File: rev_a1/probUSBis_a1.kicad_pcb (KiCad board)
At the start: 2 copper layers, 44.5 x 22.9 mm, 25 parts, among them CON1 USB-MINI-B, IC1 ATTINY85-P, P1 USB_A_MALE, P2 CONN_8, P3 CONN_4, U1 LM78L05ACZ

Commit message: added oshw logo to board
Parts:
- added G***: LOGO, LOGO, B.Cu at (118.1, 97.8)
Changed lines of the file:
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@@
     (tracks 183)
     (zones 0)
-    (modules 25)
+    (modules 26)
     (nets 21)
   )
@@
       (xy 2.71018 0) (xy 2.71018 1.016) (xy 2.71018 2.032) (xy 2.71018 2.032)) (layer B.SilkS) (width 0.00254))
   )
+  (module LOGO (layer B.Cu)
+    (at 118.11 97.79)
+    (fp_text reference G*** (at 0 -5.334) (layer B.SilkS) hide
+      (effects (font (thickness 0.3048)) (justify mirror))
+    )
+    (fp_text value LOGO (at 0 5.334) (layer B.SilkS) hide
+      (effects (font (thickness 0.3048)) (justify mirror))
+    )
+    (fp_poly (pts (xy 5.461 -4.53136) (xy 0.0635 -4.51104) (xy -5.334 -4.48818) (xy -5.35686 0.10414)
+      (xy -5.37718 4.699) (xy -5.3975 0.0635) (xy -5.41782 -4.572) (xy 0.02032 -4.55168)
+      (xy 5.461 -4.53136) (xy 5.461 -4.53136)) (layer B.SilkS) (width 0.00254))
+    (fp_poly (pts (xy 4.572 1.0922) (xy 4.2545 1.14808) (xy 3.86588 1.21666) (xy 3.60934 1.27254)
+      (xy 3.44678 1.34112) (xy 3.34264 1.44272) (xy 3.26136 1.59766) (xy 3.175 1.80848)
+      (xy 2.9718 2.30632) (xy 3.32486 2.80416) (xy 3.67538 3.302) (xy 3.25882 3.72364)
+      (xy 3.04292 3.93446) (xy 2.8702 4.08686) (xy 2.77622 4.14782) (xy 2.77368 4.14782)
+      (xy 2.67462 4.10464) (xy 2.4765 3.99034) (xy 2.24282 3.84048) (xy 1.98628 3.67538)
+      (xy 1.8161 3.59664) (xy 1.68148 3.58902) (xy 1.53416 3.63474) (xy 1.52146 3.63982)
+      (xy 1.34112 3.70332) (xy 1.2446 3.71602) (xy 1.23952 3.71348) (xy 1.20142 3.62712)
+      (xy 1.10998 3.4163) (xy 0.98298 3.10896) (xy 0.83058 2.74066) (xy 0.81788 2.70764)
+      (xy 0.41656 1.73482) (xy 0.63754 1.55702) (xy 0.96012 1.2065) (xy 1.14554 0.80772)
+      (xy 1.19634 0.38862) (xy 1.11252 -0.01778) (xy 0.89916 -0.381) (xy 0.55626 -0.66548)
+      (xy 0.508 -0.69088) (xy 0.08636 -0.83058) (xy -0.3302 -0.82042) (xy -0.7112 -0.67818)
+      (xy -1.0287 -0.42418) (xy -1.25222 -0.07366) (xy -1.35128 0.3556) (xy -1.35382 0.43942)
+      (xy -1.32588 0.82296) (xy -1.21412 1.11252) (xy -0.9906 1.38176) (xy -0.88138 1.48082)
+      (xy -0.59182 1.73482) (xy -0.98044 2.667) (xy -1.13792 3.0353) (xy -1.27762 3.34772)
+      (xy -1.38176 3.5687) (xy -1.4351 3.66522) (xy -1.5494 3.683) (xy -1.72212 3.62966)
+      (xy -1.85674 3.58394) (xy -1.99136 3.59664) (xy -2.16916 3.683) (xy -2.41046 3.83794)
+      (xy -2.65938 3.99542) (xy -2.85242 4.10718) (xy -2.94386 4.14782) (xy -3.03276 4.09194)
+      (xy -3.20294 3.94462) (xy -3.41884 3.73634) (xy -3.429 3.72618) (xy -3.84302 3.302)
+      (xy -3.49504 2.79654) (xy -3.14452 2.28854) (xy -3.36042 1.78562) (xy -3.48488 1.51384)
+      (xy -3.58648 1.3589) (xy -3.71094 1.28016) (xy -3.8989 1.23952) (xy -3.97002 1.22936)
+      (xy -4.3307 1.17602) (xy -4.55676 1.12268) (xy -4.68122 1.03886) (xy -4.73202 0.89154)
+      (xy -4.74218 0.65024) (xy -4.74218 0.45974) (xy -4.74218 -0.16256) (xy -4.42468 -0.25146)
+      (xy -4.15544 -0.30988) (xy -3.91668 -0.34036) (xy -3.89382 -0.34036) (xy -3.70078 -0.36068)
+      (xy -3.56108 -0.4445) (xy -3.43916 -0.61976) (xy -3.30454 -0.90678) (xy -3.11658 -1.3462)
+      (xy -3.47726 -1.86182) (xy -3.84048 -2.37998) (xy -3.3909 -2.83464) (xy -2.93878 -3.29184)
+      (xy -2.39268 -2.92354) (xy -1.84658 -2.55778) (xy -1.4097 -2.75844) (xy -0.97282 -2.9591)
+      (xy -0.85344 -3.59918) (xy -0.73152 -4.2418) (xy -0.09652 -4.2164) (xy 0.54102 -4.191)
+      (xy 0.6731 -3.56616) (xy 0.80518 -2.94132) (xy 1.2446 -2.74828) (xy 1.68402 -2.55524)
+      (xy 2.21742 -2.92862) (xy 2.75082 -3.29946) (xy 3.20548 -2.84734) (xy 3.66014 -2.39268)
+      (xy 3.30454 -1.86944) (xy 2.95148 -1.3462) (xy 3.14198 -0.88646) (xy 3.25628 -0.62738)
+      (xy 3.37058 -0.47244) (xy 3.53314 -0.38354) (xy 3.79222 -0.32512) (xy 3.937 -0.29972)
+      (xy 4.2545 -0.24638) (xy 4.44246 -0.18542) (xy 4.53644 -0.07366) (xy 4.56946 0.127)
+      (xy 4.572 0.45466) (xy 4.572 0.46736) (xy 4.572 1.0922) (xy 4.572 1.0922)) (layer B.SilkS) (width 0.00254))
+  )
   (gr_text SCK (at 143.51 99.06 270) (layer B.SilkS)
     (effects (font (size 0.4 0.4) (thickness 0.1)) (justify mirror))
@@
     (effects (font (size 0.8 0.8) (thickness 0.16)) (justify mirror))
   )
-  (gr_text github.com/emdarcher/probUSBis_hardware (at 113.03 102.87 90) (layer B.SilkS)
+  (gr_text github.com/emdarcher/probUSBis_hardware (at 111.76 102.87 90) (layer B.SilkS)
     (effects (font (size 0.6 0.6) (thickness 0.12)) (justify mirror))
   )

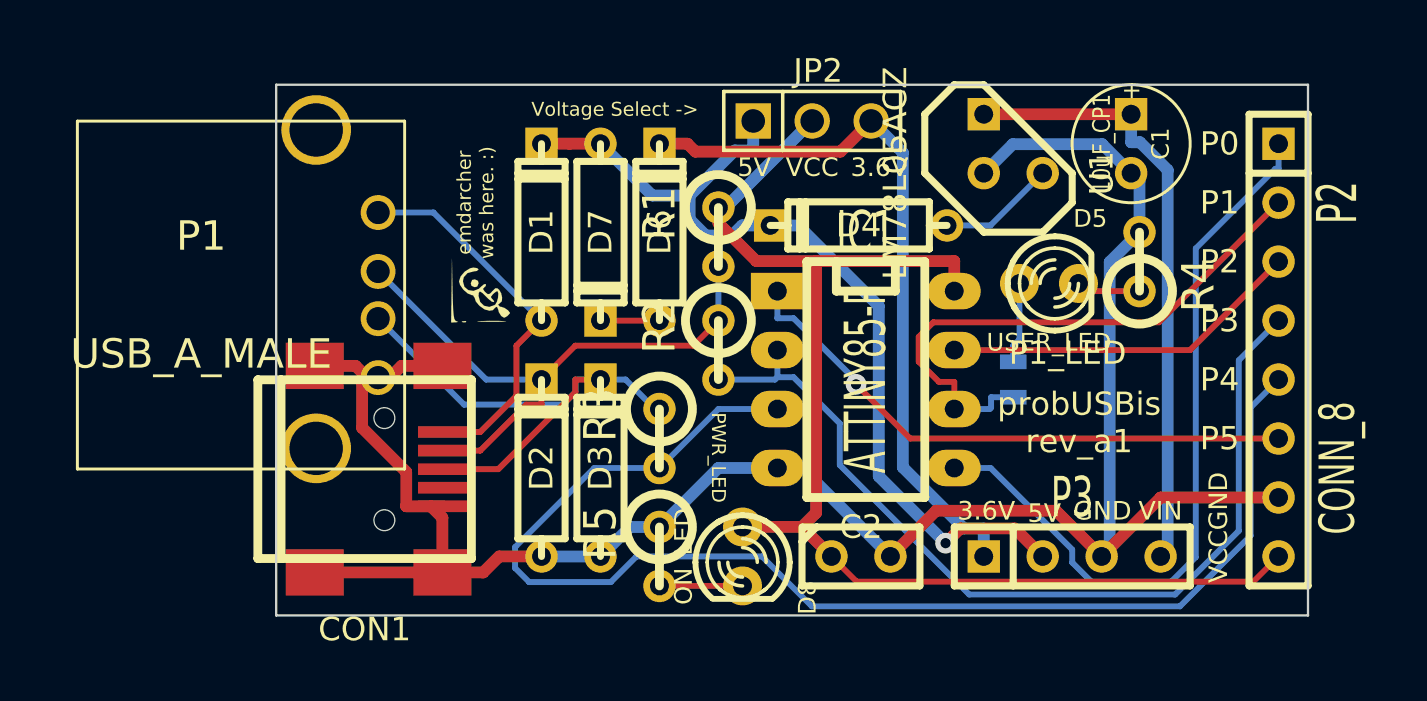
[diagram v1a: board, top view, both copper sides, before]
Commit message: added a ground fill
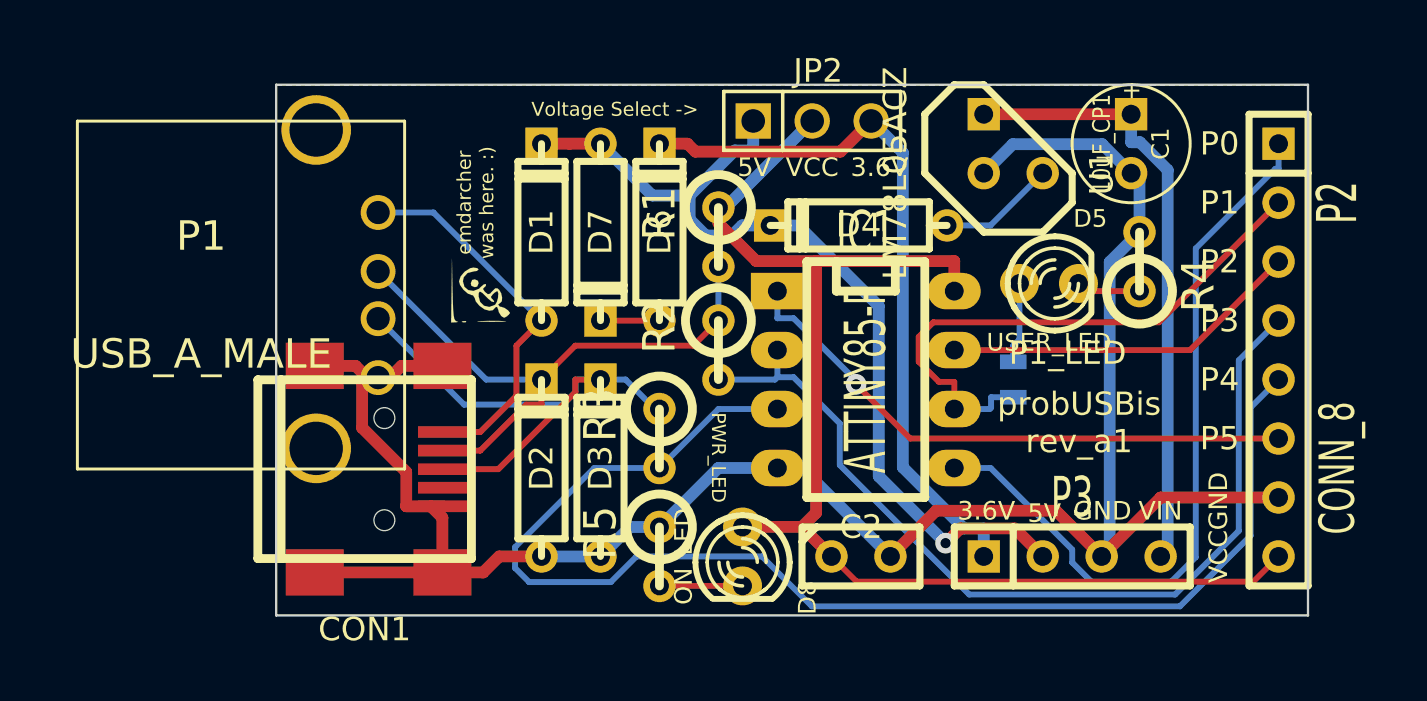
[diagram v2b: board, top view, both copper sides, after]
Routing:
- added copper zone on B.Cu, net GND
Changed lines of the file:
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@@
       (xy 4.572 0.45466) (xy 4.572 0.46736) (xy 4.572 1.0922) (xy 4.572 1.0922)) (layer B.SilkS) (width 0.00254))
   )
+  (gr_line (start 105.41 114.3) (end 105.41 91.44) (angle 90) (layer Edge.Cuts) (width 0.1))
+  (gr_line (start 149.86 114.3) (end 105.41 114.3) (angle 90) (layer Edge.Cuts) (width 0.1))
+  (gr_line (start 149.86 91.44) (end 149.86 114.3) (angle 90) (layer Edge.Cuts) (width 0.1))
+  (gr_line (start 105.41 91.44) (end 149.86 91.44) (angle 90) (layer Edge.Cuts) (width 0.1))
   (gr_text SCK (at 143.51 99.06 270) (layer B.SilkS)
     (effects (font (size 0.4 0.4) (thickness 0.1)) (justify mirror))
@@
     (effects (font (size 1 1) (thickness 0.25)))
   )
-  (gr_line (start 149.86 91.44) (end 105.41 91.44) (angle 90) (layer Edge.Cuts) (width 0.1))
-  (gr_line (start 149.86 114.3) (end 149.86 91.44) (angle 90) (layer Edge.Cuts) (width 0.1))
-  (gr_line (start 105.41 114.3) (end 149.86 114.3) (angle 90) (layer Edge.Cuts) (width 0.1))
-  (gr_line (start 105.41 91.44) (end 105.41 114.3) (angle 90) (layer Edge.Cuts) (width 0.1))
   (segment (start 123.4691 94.3223) (end 123.1268 93.98) (width 0.508) (layer F.Cu) (net 1))
   (segment (start 129.7177 94.3223) (end 123.4691 94.3223) (width 0.508) (layer F.Cu) (net 1))
@@
   (segment (start 142.6171 93.9168) (end 143.8156 95.1153) (width 0.508) (layer B.Cu) (net 20))
   (segment (start 142.24 93.9168) (end 142.6171 93.9168) (width 0.508) (layer B.Cu) (net 20))
+  (zone (net 3) (net_name GND) (layer B.Cu) (hatch edge 0.508)
+    (connect_pads (clearance 0.508))
+    (min_thickness 0.254)
+    (fill (arc_segments 16) (thermal_gap 0.508) (thermal_bridge_width 0.255))
+    (polygon
+      (pts
+        (xy 149.86 114.3) (xy 105.41 114.3) (xy 105.41 91.44) (xy 149.86 91.44)
+      )
+    )
+  )
 )
